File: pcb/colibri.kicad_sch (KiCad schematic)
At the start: 55 parts

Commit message: basic layout
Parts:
- ld-1, ld-10, ld-11, ld-12, ld-13, ld-14, ld-15, ld-16, ld-17, ld-18, ld-19, ld-2, ld-20, ld-21, ld-22, ld-23, ld-24, ld-25, ld-26, ld-27, ld-3, ld-4, ld-5, ld-6, ld-7, ld-8, ld-9: footprint kbd:D3_SMD_v2 -> kbd:D3_TH_SMD_v2
- lsw-1, lsw-13, lsw-19, lsw-7: footprint kbd:CherryMX_Hotswap_1.5u -> kbd:CherryMX_Hotswap_1.25U
- pro-micro1: renamed from left-pro-micro1; footprint kbd:ProMicro_v3.5 -> kbd:ProMicro_v4
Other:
- moved on the sheet: pro-micro1

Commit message: diodes on place
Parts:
- ld-1, ld-10, ld-11, ld-12, ld-13, ld-14, ld-15, ld-16, ld-17, ld-18, ld-19, ld-2, ld-20, ld-21, ld-22, ld-23, ld-24, ld-25, ld-26, ld-27, ld-3, ld-4, ld-5, ld-6, ld-7, ld-8, ld-9: footprint kbd:D3_TH_SMD_v2 -> kbd:D3_SMD_v2

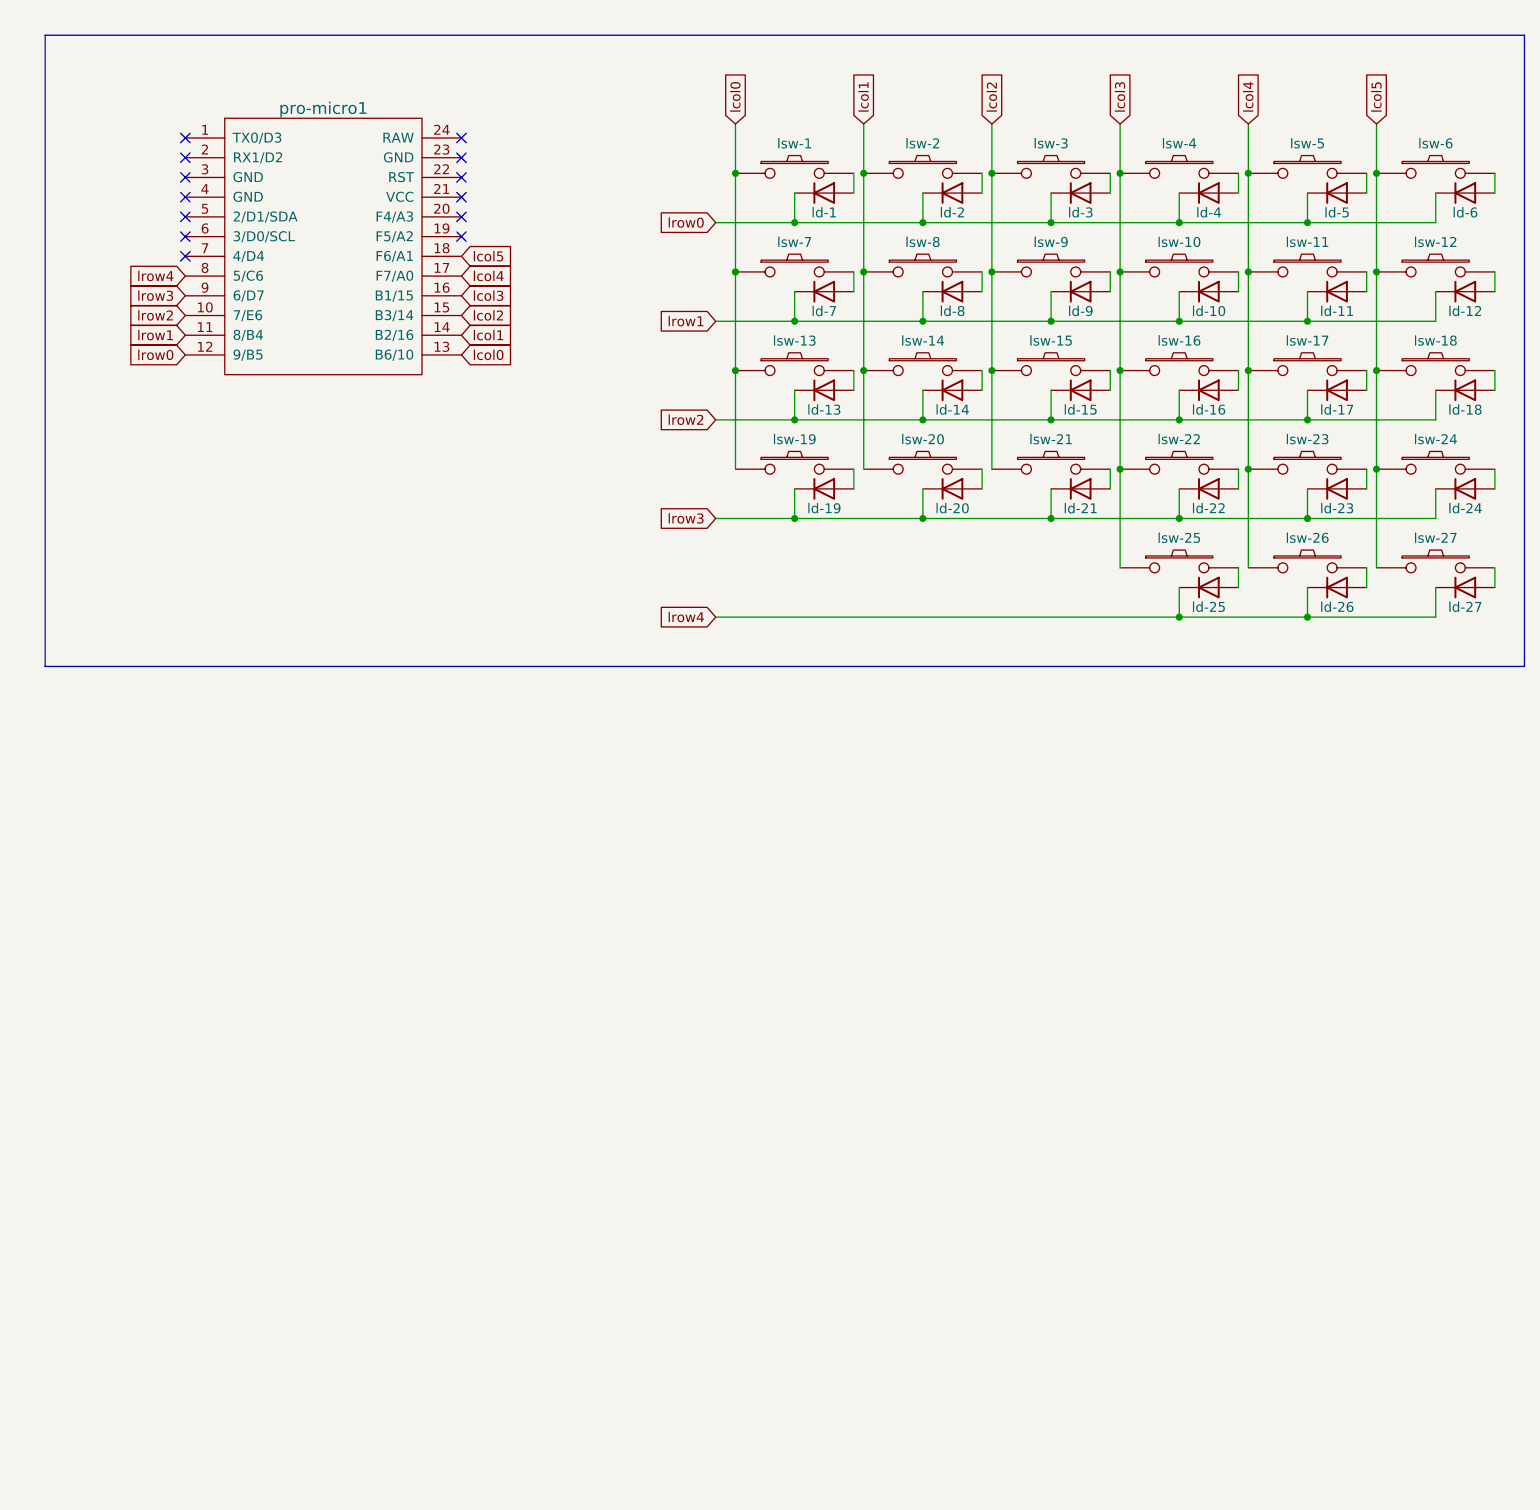
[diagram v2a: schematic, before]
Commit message: schematics almost finished for left side
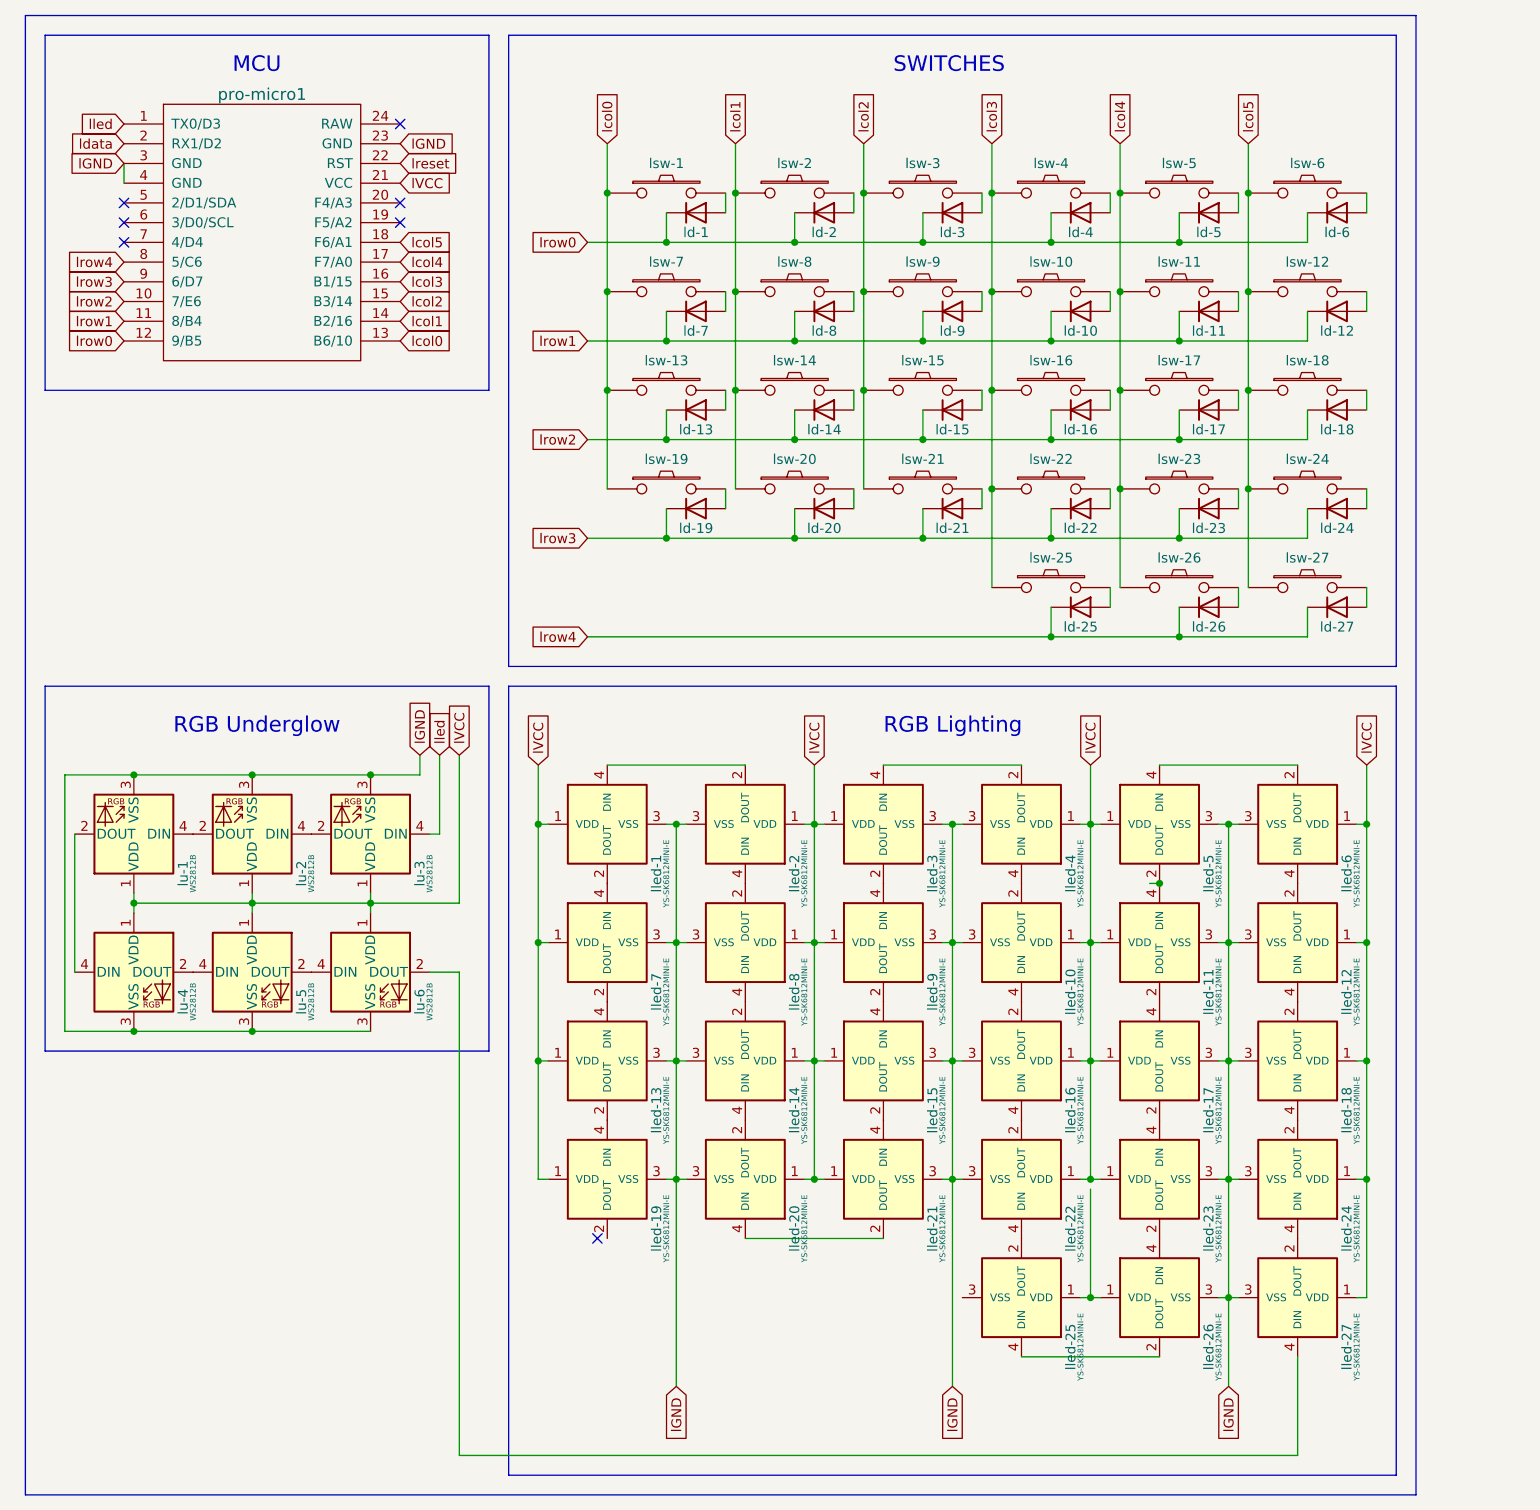
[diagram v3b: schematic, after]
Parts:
- added lled-1, lled-10, lled-11, lled-12, lled-13, lled-14, lled-15, lled-16, lled-17, lled-18, lled-19, lled-2, lled-20, lled-21, lled-22, lled-23, lled-24, lled-25, lled-26, lled-27, lled-3, lled-4, lled-5, lled-6, lled-7, lled-8, lled-9: YS-SK6812MINI-E, symbol kbd:YS-SK6812MINI-E
- added lu-1, lu-2, lu-3, lu-4, lu-5, lu-6: WS2812B, LED_SMD:LED_WS2812B_PLCC4_5.0x5.0mm_P3.2mm, symbol LED:WS2812B
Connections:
- net lled: now reaches pro-micro1.1 (TX0/D3)
- net lled: now also lu-3.4 (DIN)
- net ldata: now reaches pro-micro1.2 (RX1/D2)
- net lVCC: now reaches pro-micro1.21 (VCC)
- net lVCC: now also lled-1.1 (VDD), lled-10.1 (VDD), lled-11.1 (VDD), lled-12.1 (VDD), lled-13.1 (VDD), lled-14.1 (VDD), lled-15.1 (VDD), lled-16.1 (VDD), lled-17.1 (VDD), lled-18.1 (VDD), lled-19.1 (VDD), lled-2.1 (VDD), lled-20.1 (VDD), lled-21.1 (VDD), lled-22.1 (VDD), lled-23.1 (VDD), lled-24.1 (VDD), lled-27.1 (VDD), lled-3.1 (VDD), lled-4.1 (VDD), lled-5.1 (VDD), lled-6.1 (VDD), lled-7.1 (VDD), lled-8.1 (VDD), lled-9.1 (VDD), lu-1.1 (VDD), lu-2.1 (VDD), lu-3.1 (VDD), lu-4.1 (VDD), lu-5.1 (VDD), lu-6.1 (VDD)
- net lreset: now reaches pro-micro1.22 (RST)
- net lGND: now reaches pro-micro1.23 (GND)
- net lGND: now also pro-micro1.3 (GND), pro-micro1.4 (GND), lled-1.3 (VSS), lled-10.3 (VSS), lled-11.3 (VSS), lled-12.3 (VSS), lled-13.3 (VSS), lled-14.3 (VSS), lled-15.3 (VSS), lled-16.3 (VSS), lled-17.3 (VSS), lled-18.3 (VSS), lled-19.3 (VSS), lled-2.3 (VSS), lled-20.3 (VSS), lled-21.3 (VSS), lled-22.3 (VSS), lled-23.3 (VSS), lled-24.3 (VSS), lled-26.3 (VSS), lled-27.3 (VSS), lled-3.3 (VSS), lled-4.3 (VSS), lled-5.3 (VSS), lled-6.3 (VSS), lled-7.3 (VSS), lled-8.3 (VSS), lled-9.3 (VSS), lu-1.3 (VSS), lu-2.3 (VSS), lu-3.3 (VSS), lu-4.3 (VSS), lu-5.3 (VSS), lu-6.3 (VSS)
- new net: lu-4.2 (DOUT), lu-5.4 (DIN)
- new net: lu-1.2 (DOUT), lu-4.4 (DIN)
- new net: lled-15.2 (DOUT), lled-21.4 (DIN)
- new net: lled-15.4 (DIN), lled-9.2 (DOUT)
- new net: lled-23.2 (DOUT), lled-26.4 (DIN)
- new net: lled-17.2 (DOUT), lled-23.4 (DIN)
- new net: lled-24.4 (DIN), lled-27.2 (DOUT)
- new net: lled-27.4 (DIN), lu-6.2 (DOUT)
- new net: lled-10.2 (DOUT), lled-4.4 (DIN)
- new net: lled-10.4 (DIN), lled-16.2 (DOUT)
- new net: lled-5.4 (DIN), lled-6.2 (DOUT)
- new net: lled-12.2 (DOUT), lled-6.4 (DIN)
- new net: lled-11.2 (DOUT), lled-17.4 (DIN)
- new net: lled-11.4 (DIN), lled-5.2 (DOUT)
- new net: lu-1.4 (DIN), lu-2.2 (DOUT)
- new net: lu-2.4 (DIN), lu-3.2 (DOUT)
- new net: lled-16.4 (DIN), lled-22.2 (DOUT)
- new net: lled-22.4 (DIN), lled-25.2 (DOUT)
- new net: lled-1.2 (DOUT), lled-7.4 (DIN)
- new net: lled-1.4 (DIN), lled-2.2 (DOUT)
- new net: lled-3.2 (DOUT), lled-9.4 (DIN)
- new net: lled-3.4 (DIN), lled-4.2 (DOUT)
- new net: lled-14.2 (DOUT), lled-8.4 (DIN)
- new net: lled-14.4 (DIN), lled-20.2 (DOUT)
- new net: lled-25.1 (VDD), lled-26.1 (VDD)
- new net: lled-25.4 (DIN), lled-26.2 (DOUT)
- new net: lled-13.2 (DOUT), lled-19.4 (DIN)
- new net: lled-13.4 (DIN), lled-7.2 (DOUT)
- new net: lu-5.2 (DOUT), lu-6.4 (DIN)
- new net: lled-2.4 (DIN), lled-8.2 (DOUT)
- new net: lled-12.4 (DIN), lled-18.2 (DOUT)
- new net: lled-18.4 (DIN), lled-24.2 (DOUT)
- new net: lled-20.4 (DIN), lled-21.2 (DOUT)
- no-connect marks 13 -> 7
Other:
- note added: "MCU"
- note added: "RGB Lighting"
- note added: "RGB Underglow"
- note added: "SWITCHES"
- moved on the sheet: ld-1, ld-10, ld-11, ld-12, ld-13, ld-14, ld-15, ld-16, ld-17, ld-18, ld-19, ld-2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

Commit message: better LED placement
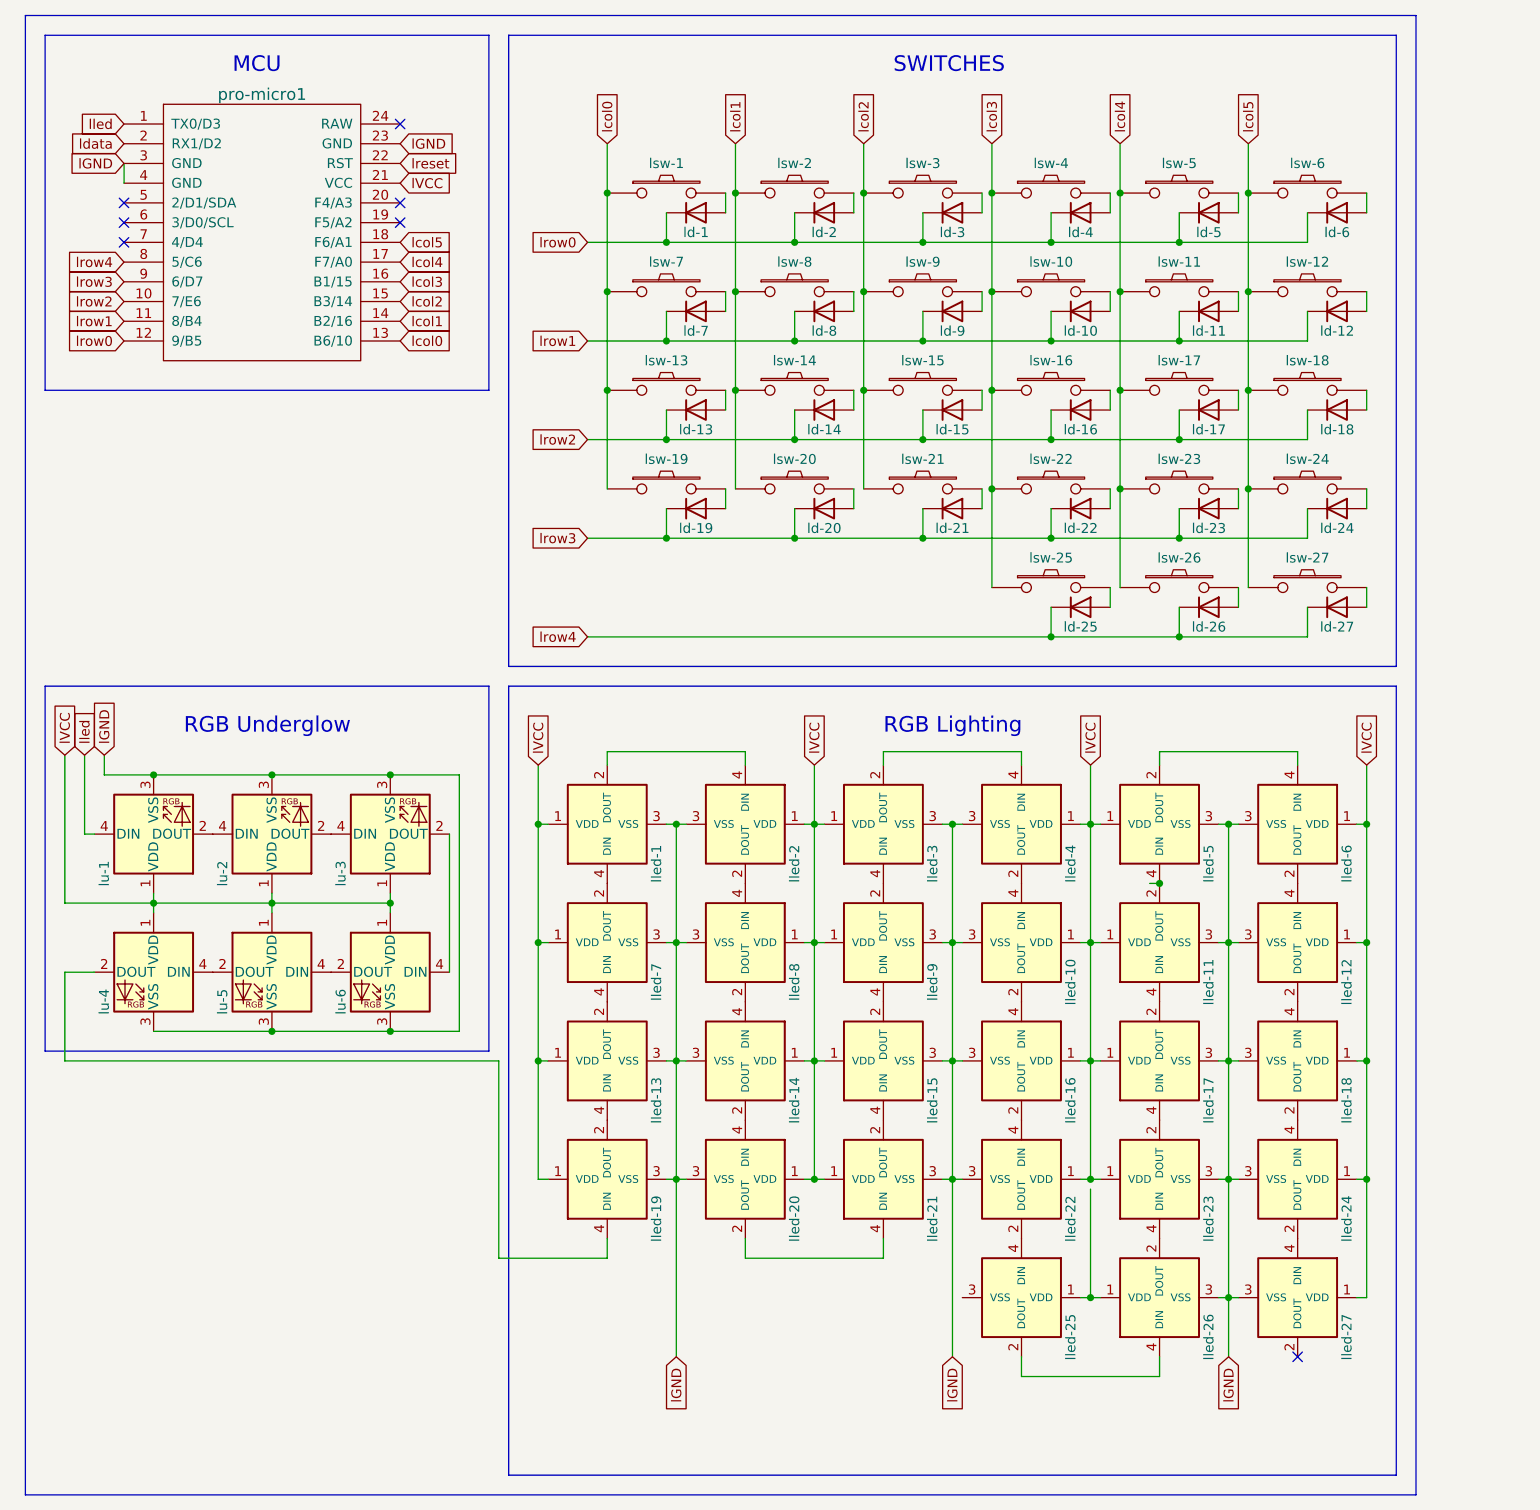
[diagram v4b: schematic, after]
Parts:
- lled-1: renamed from lled-19; footprint (none) -> kbd:YS-SK6812MINI-E
- lled-10: renamed from lled-22; footprint (none) -> kbd:YS-SK6812MINI-E
- lled-11: renamed from lled-23; footprint (none) -> kbd:YS-SK6812MINI-E
- lled-12: renamed from lled-24; footprint (none) -> kbd:YS-SK6812MINI-E
- lled-13: renamed from lled-7; footprint (none) -> kbd:YS-SK6812MINI-E
- lled-14: renamed from lled-8; footprint (none) -> kbd:YS-SK6812MINI-E
- lled-15: renamed from lled-9; footprint (none) -> kbd:YS-SK6812MINI-E
- lled-16, lled-17, lled-18: footprint (none) -> kbd:YS-SK6812MINI-E
- lled-19: renamed from lled-1; footprint (none) -> kbd:YS-SK6812MINI-E
- lled-2: renamed from lled-20; footprint (none) -> kbd:YS-SK6812MINI-E
- lled-20: renamed from lled-2; footprint (none) -> kbd:YS-SK6812MINI-E
- lled-21: renamed from lled-3; footprint (none) -> kbd:YS-SK6812MINI-E
- lled-22: renamed from lled-10; footprint (none) -> kbd:YS-SK6812MINI-E
- lled-23: renamed from lled-11; footprint (none) -> kbd:YS-SK6812MINI-E
- lled-24: renamed from lled-12; footprint (none) -> kbd:YS-SK6812MINI-E
- lled-25: renamed from lled-4; footprint (none) -> kbd:YS-SK6812MINI-E
- lled-26: renamed from lled-5; footprint (none) -> kbd:YS-SK6812MINI-E
- lled-27: renamed from lled-6; footprint (none) -> kbd:YS-SK6812MINI-E
- lled-3: renamed from lled-21; footprint (none) -> kbd:YS-SK6812MINI-E
- lled-4: renamed from lled-25; footprint (none) -> kbd:YS-SK6812MINI-E
- lled-5: renamed from lled-26; footprint (none) -> kbd:YS-SK6812MINI-E
- lled-6: renamed from lled-27; footprint (none) -> kbd:YS-SK6812MINI-E
- lled-7: renamed from lled-13; footprint (none) -> kbd:YS-SK6812MINI-E
- lled-8: renamed from lled-14; footprint (none) -> kbd:YS-SK6812MINI-E
- lled-9: renamed from lled-15; footprint (none) -> kbd:YS-SK6812MINI-E
- renumbered lu-3 to lu-1, lu-1 to lu-3, lu-6 to lu-4, lu-4 to lu-6
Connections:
- net lGND: now also lled-4.3 (VSS); no longer lled-25.3 (VSS)
- net lVCC: now also lled-4.1 (VDD), lled-5.1 (VDD); no longer lled-25.1 (VDD), lled-26.1 (VDD)
- net at lled-6.4 (DIN): now also lled-5.2 (DOUT); no longer lu-4.2 (DOUT)
- net at lled-27.2 (DOUT): no longer lled-26.4 (DIN)
- net at lled-19.4 (DIN): now also lu-4.2 (DOUT); no longer lled-20.2 (DOUT)
- net at lled-21.4 (DIN): now also lled-20.2 (DOUT); no longer lled-25.2 (DOUT)
- net at lled-4.4 (DIN): now also lled-3.2 (DOUT); no longer lled-5.2 (DOUT)
- net at lled-1.2 (DOUT): now also lled-2.4 (DIN)
- new net: lled-25.1 (VDD), lled-26.1 (VDD)
- new net: lled-25.2 (DOUT), lled-26.4 (DIN)
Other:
- moved on the sheet: lled-1, lled-10, lled-11, lled-12, lled-13, lled-14, lled-15, lled-19, lled-2, lled-20, lled-21, lled-22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
